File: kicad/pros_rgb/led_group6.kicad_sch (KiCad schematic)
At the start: 8 parts

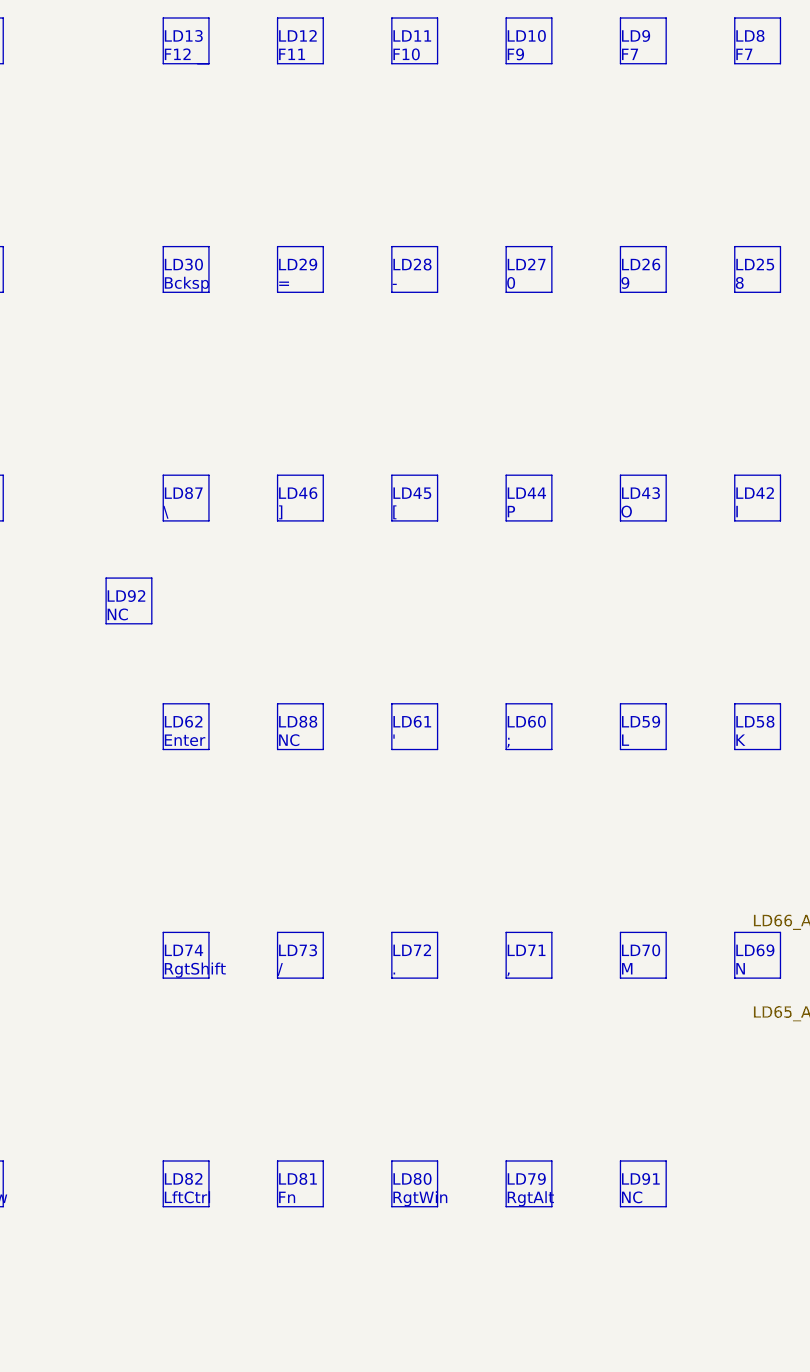
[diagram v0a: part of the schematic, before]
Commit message: kicad/pros_rgb: fix typos
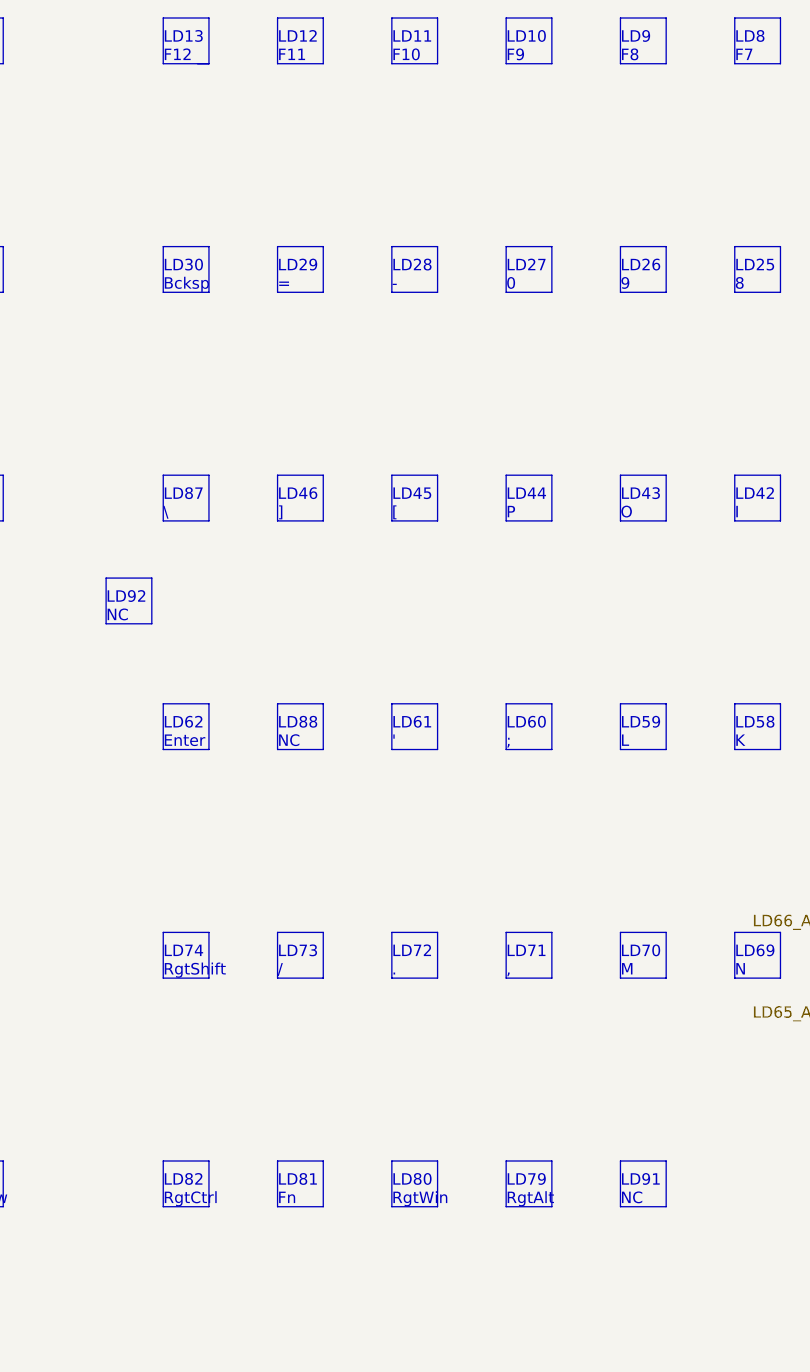
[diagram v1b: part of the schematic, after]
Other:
- note added: "LD82 RgtCtrl"
- note added: "LD9 F8"
- note removed: "LD82 LftCtrl"
- note removed: "LD9 F7"
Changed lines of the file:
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@@
     (effects (font (size 1.27 1.27)) (justify left bottom))
   )
-  (text "LD82\nLftCtrl" (at 106.68 156.21 0)
+  (text "LD82\nRgtCtrl" (at 106.68 156.21 0)
     (effects (font (size 1.27 1.27)) (justify left bottom))
   )
@@
     (effects (font (size 1.27 1.27)) (justify left bottom))
   )
-  (text "LD9\nF7" (at 157.48 29.21 0)
+  (text "LD9\nF8" (at 157.48 29.21 0)
     (effects (font (size 1.27 1.27)) (justify left bottom))
   )

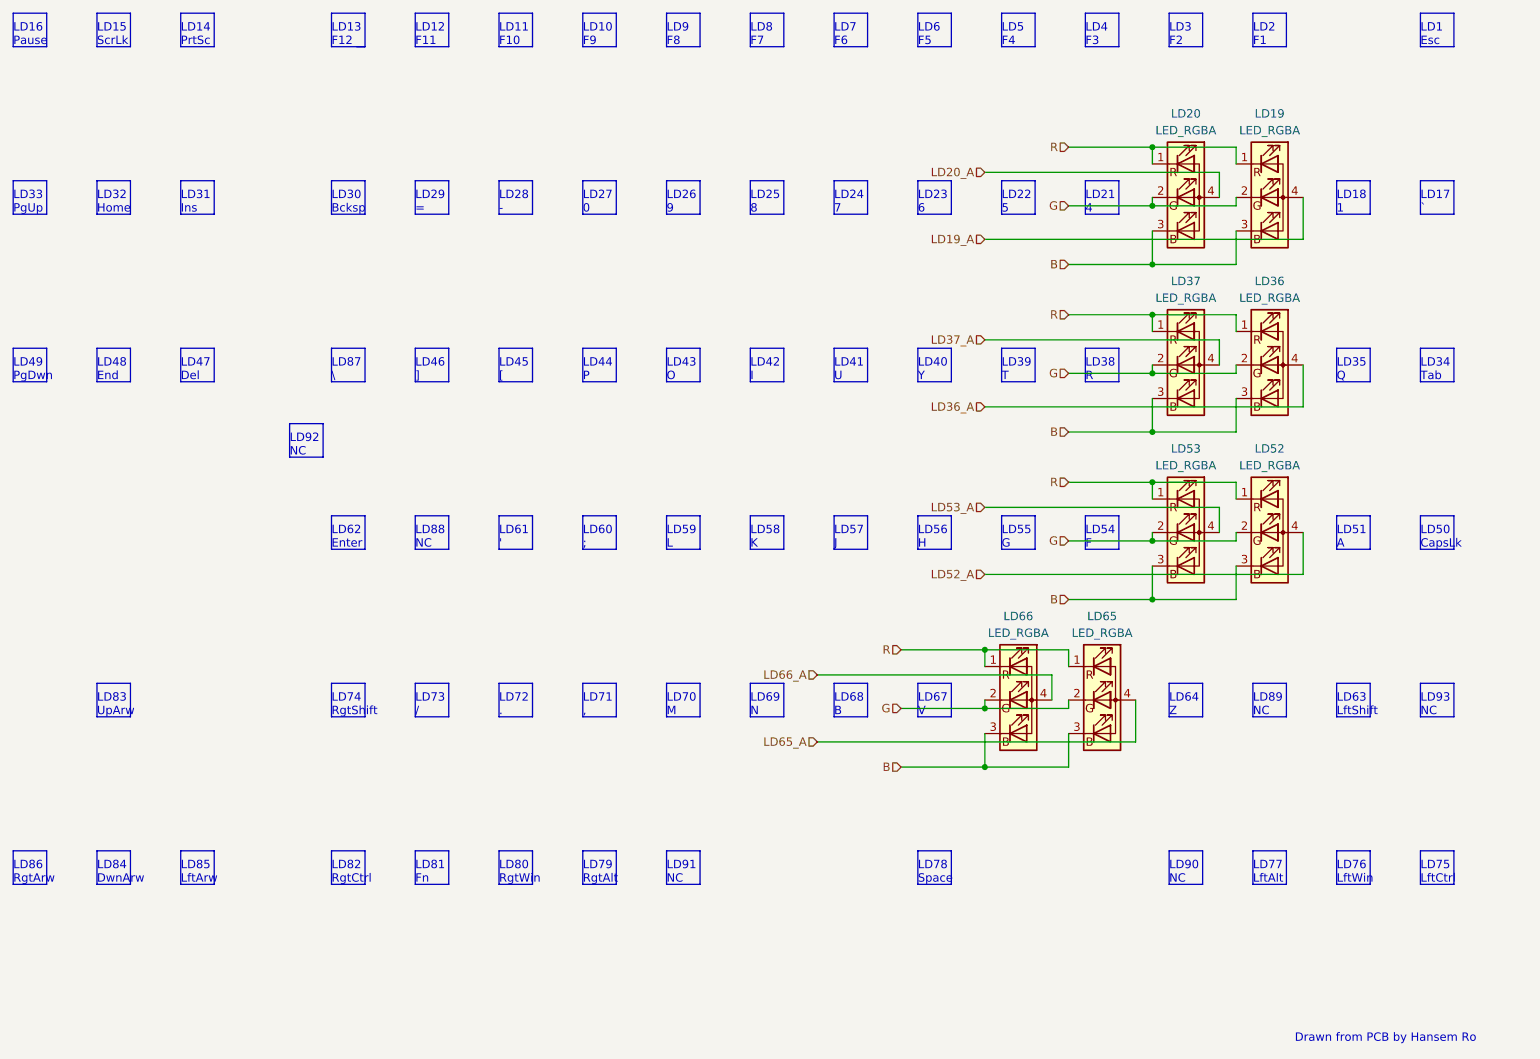
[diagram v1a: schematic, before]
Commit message: kicad/pros_rgb: order led groups by channel number
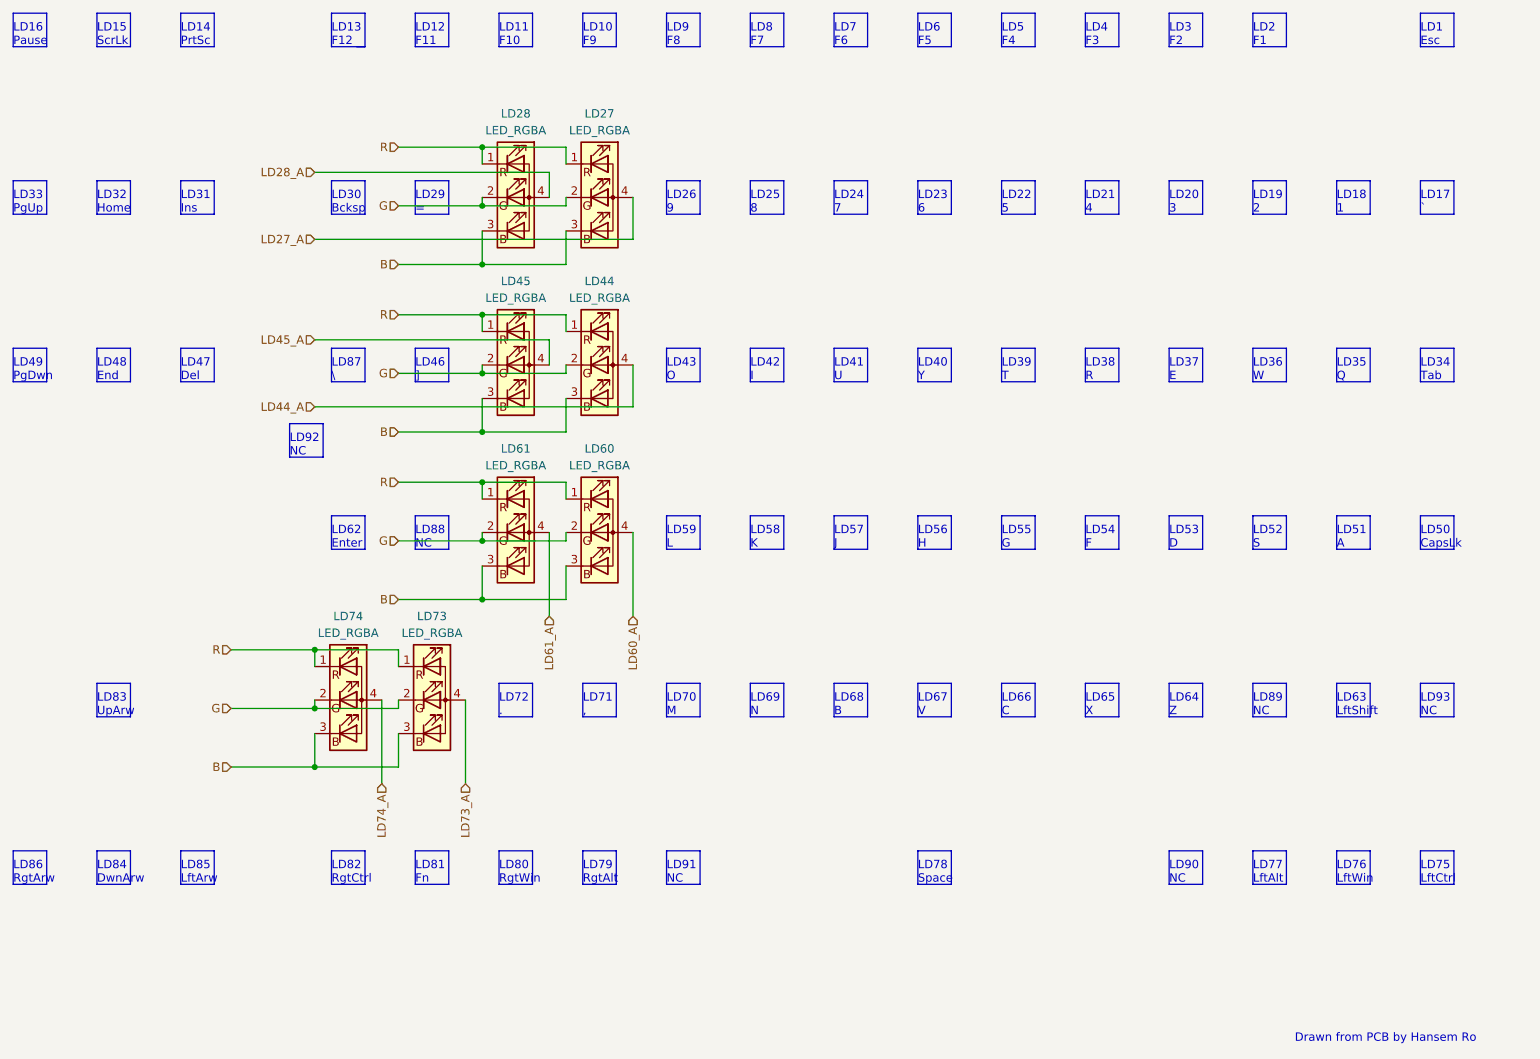
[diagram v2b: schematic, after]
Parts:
- removed LD19, LD20, LD36, LD37, LD52, LD53, LD65, LD66: LED_RGBA, symbol Device:LED_RGBA
- added LD27, LD28, LD44, LD45, LD60, LD61, LD73, LD74: LED_RGBA, symbol Device:LED_RGBA
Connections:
- net B: now also LD27.3 (BK), LD28.3 (BK), LD44.3 (BK), LD45.3 (BK), LD60.3 (BK), LD61.3 (BK), LD73.3 (BK), LD74.3 (BK)
- net G: now also LD27.2 (GK), LD28.2 (GK), LD44.2 (GK), LD45.2 (GK), LD60.2 (GK), LD61.2 (GK), LD73.2 (GK), LD74.2 (GK)
- net R: now also LD27.1 (RK), LD28.1 (RK), LD44.1 (RK), LD45.1 (RK), LD60.1 (RK), LD61.1 (RK), LD73.1 (RK), LD74.1 (RK)
- new net LD27_A: LD27.4 (A)
- new net LD28_A: LD28.4 (A)
- new net LD44_A: LD44.4 (A)
- new net LD45_A: LD45.4 (A)
- new net LD60_A: LD60.4 (A)
- new net LD61_A: LD61.4 (A)
- new net LD73_A: LD73.4 (A)
- new net LD74_A: LD74.4 (A)
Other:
- note added: "LD19 2"
- note added: "LD20 3"
- note added: "LD36 W"
- note added: "LD37 E"
- note added: "LD52 S"
- note added: "LD53 D"
- note added: "LD65 X"
- note added: "LD66 C"
- note removed: "LD27 0"
- note removed: "LD28 -"
- note removed: "LD44 P"
- note removed: "LD45 ["
- note removed: "LD60 ;"
- note removed: "LD61 '"
- note removed: "LD73 /"
- note removed: "LD74 RgtShift"
